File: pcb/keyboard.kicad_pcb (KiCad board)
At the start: 2 copper layers, 232.6 x 118.3 mm, 123 parts, among them SW1 Push, SW10 Push, SW11 Push, SW12 Push, SW14 Push, SW15 Push, SW16 Push, SW17 Push, SW18 Push, SW2 Push, SW20 Push, SW21 Push, SW22 Push, SW23 Push, SW24 Push, SW26 Push, SW27 Push, SW28 Push, SW29 Push, SW3 Push, SW30 Push, SW32 Push, SW33 Push, SW34 Push, SW35 Push, SW38 Push, SW39 Push, SW4 Push, SW40 Push, SW41 Push, SW42 Push, SW44 Push, SW45 Push, SW46 Push, SW47 Push, SW48 Push, SW5 Push, SW50 Push, SW51 Push, SW52 Push, SW53 Push, SW54 Push, SW56 Push, SW57 Push, SW58 Push, SW59 Push, SW6 Push, SW60 Push, SW62 Push, SW63 Push, SW64 Push, SW65 Push, SW66 Push, SW67 Push, SW68 Push, SW69 Push, SW70 Push, SW71 Push, SW72 Push, SW8 Push, SW9 Push, U1 Arduino_Pro_Micro

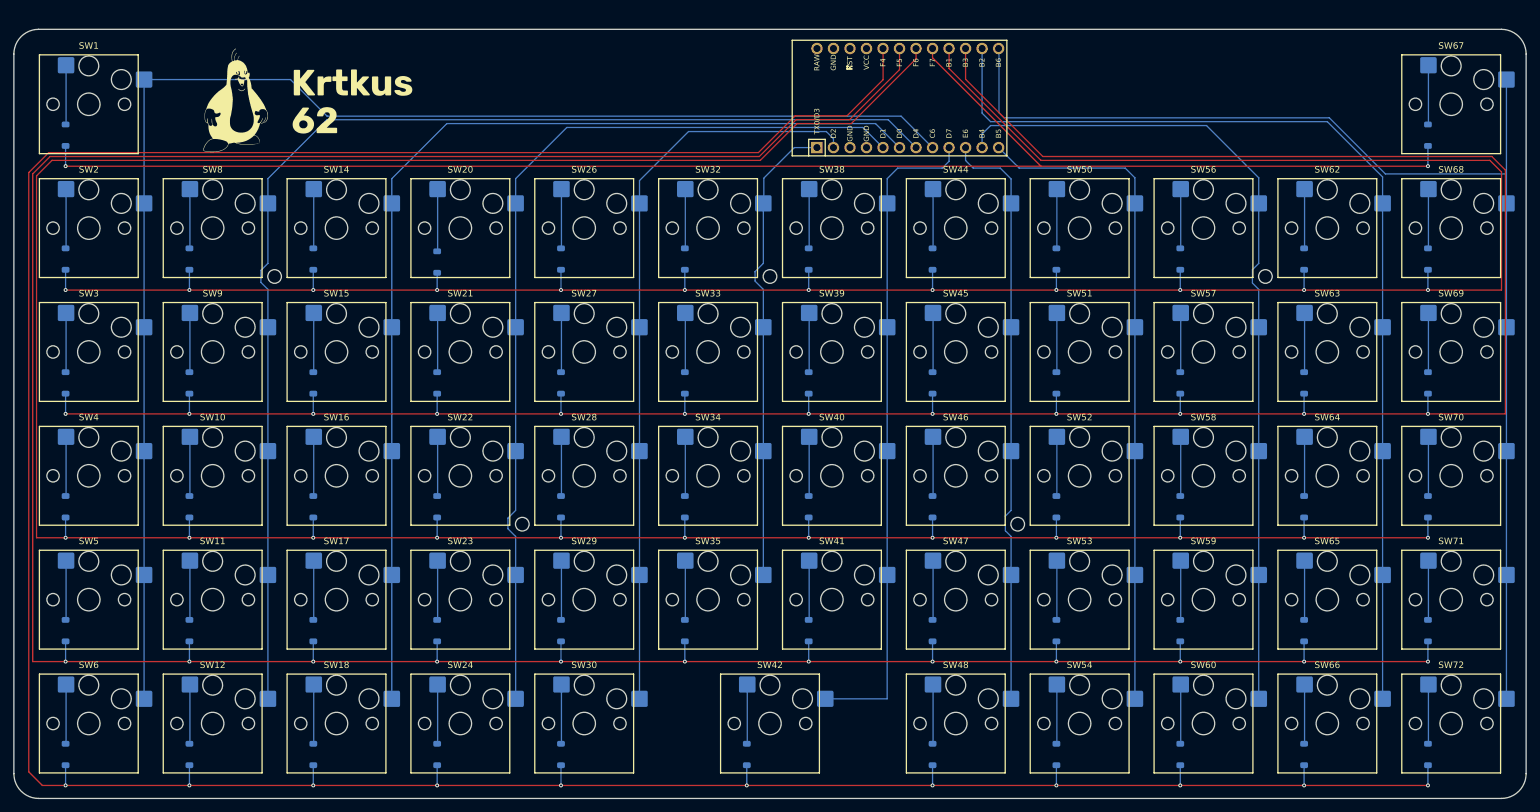
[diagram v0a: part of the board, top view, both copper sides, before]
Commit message: remove switch labels
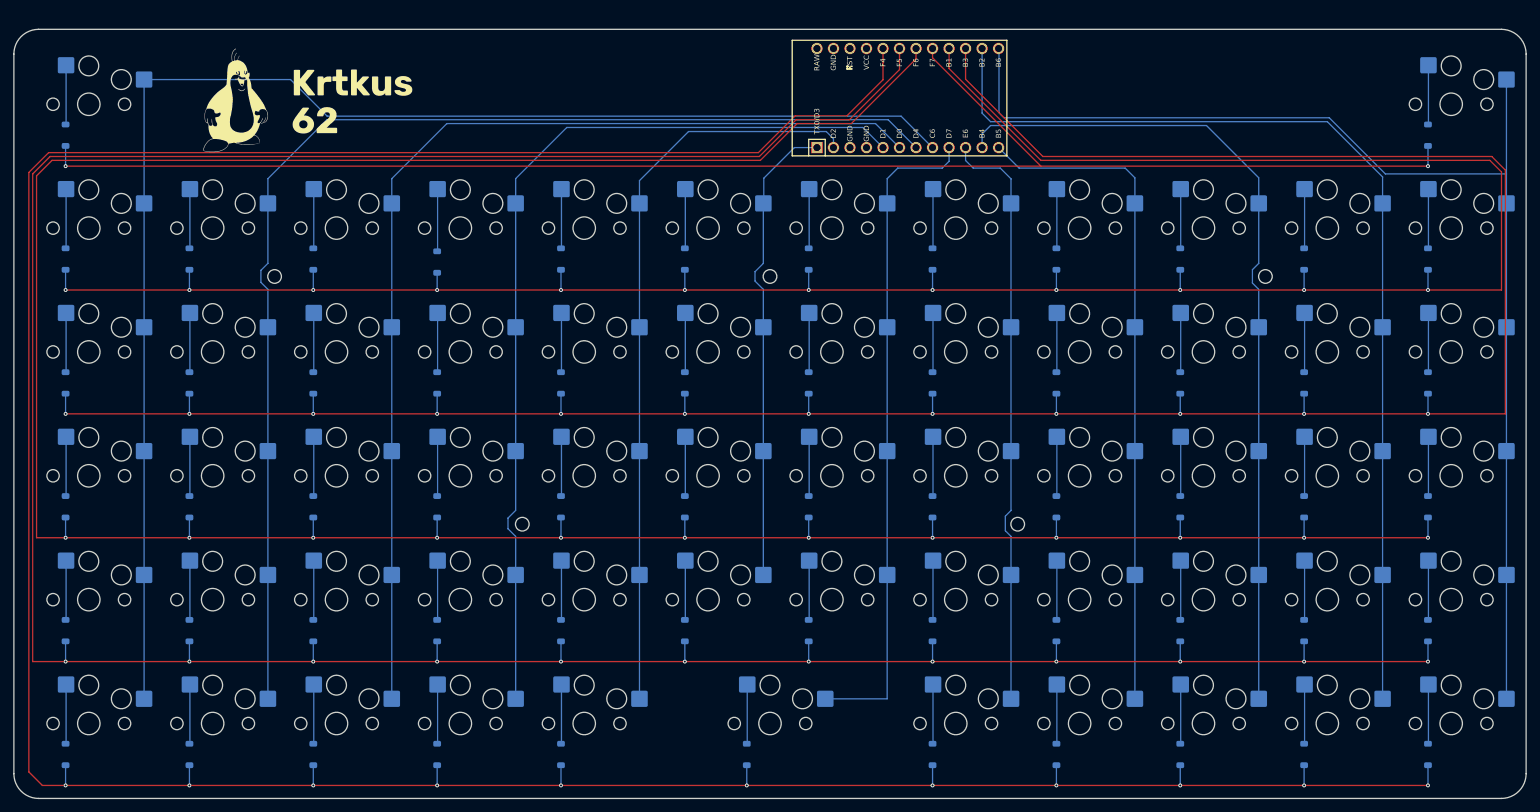
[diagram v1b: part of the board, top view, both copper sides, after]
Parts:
- SW1, SW10, SW11, SW12, SW14, SW15, SW16, SW17, SW18, SW2, SW20, SW21, SW22, SW23, SW24, SW26, SW27, SW28, SW29, SW3, SW30, SW32, SW33, SW34, SW35, SW38, SW39, SW4, SW40, SW41, SW42, SW44, SW45, SW46, SW47, SW48, SW5, SW50, SW51, SW52, SW53, SW54, SW56, SW57, SW58, SW59, SW6, SW60, SW62, SW63, SW64, SW65, SW66, SW67, SW68, SW69, SW70, SW71, SW72, SW8, SW9: footprint ScottoKeebs_Hotswap:Hotswap_Choc_V1_1.00u -> ScottoKeebs_Hotswap:Hotswap_Choc_V1_1.00u_No_Silkscreen

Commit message: through hole
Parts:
- SW1, SW10, SW11, SW12, SW14, SW15, SW16, SW17, SW18, SW2, SW20, SW21, SW22, SW23, SW24, SW26, SW27, SW28, SW29, SW3, SW30, SW32, SW33, SW34, SW35, SW38, SW39, SW4, SW40, SW41, SW42, SW44, SW45, SW46, SW47, SW48, SW5, SW50, SW51, SW52, SW53, SW54, SW56, SW57, SW58, SW59, SW6, SW60, SW62, SW63, SW64, SW65, SW66, SW67, SW68, SW69, SW70, SW71, SW72, SW8, SW9: footprint ScottoKeebs_Hotswap:Hotswap_Choc_V1_1.00u_No_Silkscreen -> ScottoKeebs_Choc:Choc_V1_1.00u_No_Label
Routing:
- net COL0: track 220.9 -> 242.9 mm
- net COL11: track 187.7 -> 208.9 mm
- net COL8: track 103.0 -> 121.6 mm
- net COL3: track 142.0 -> 160.6 mm
- net COL2: track 163.1 -> 181.7 mm
- net COL1: track 186.1 -> 204.6 mm
- net COL4: track 114.5 -> 133.0 mm
- net COL9: track 129.5 -> 148.0 mm
- net COL10: track 156.6 -> 175.1 mm
- net COL7: track 90.8 -> 109.3 mm
- net COL6: track 102.3 -> 120.0 mm
- net COL5: track 72.2 -> 86.8 mm
- net Net-(D8-A): track 9.14 -> 10.5 mm
- net Net-(D71-A): track 9.14 -> 10.5 mm
- net Net-(D70-A): track 9.14 -> 10.5 mm
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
